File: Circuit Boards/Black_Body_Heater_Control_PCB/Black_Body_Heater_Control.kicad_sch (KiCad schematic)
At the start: 0 parts

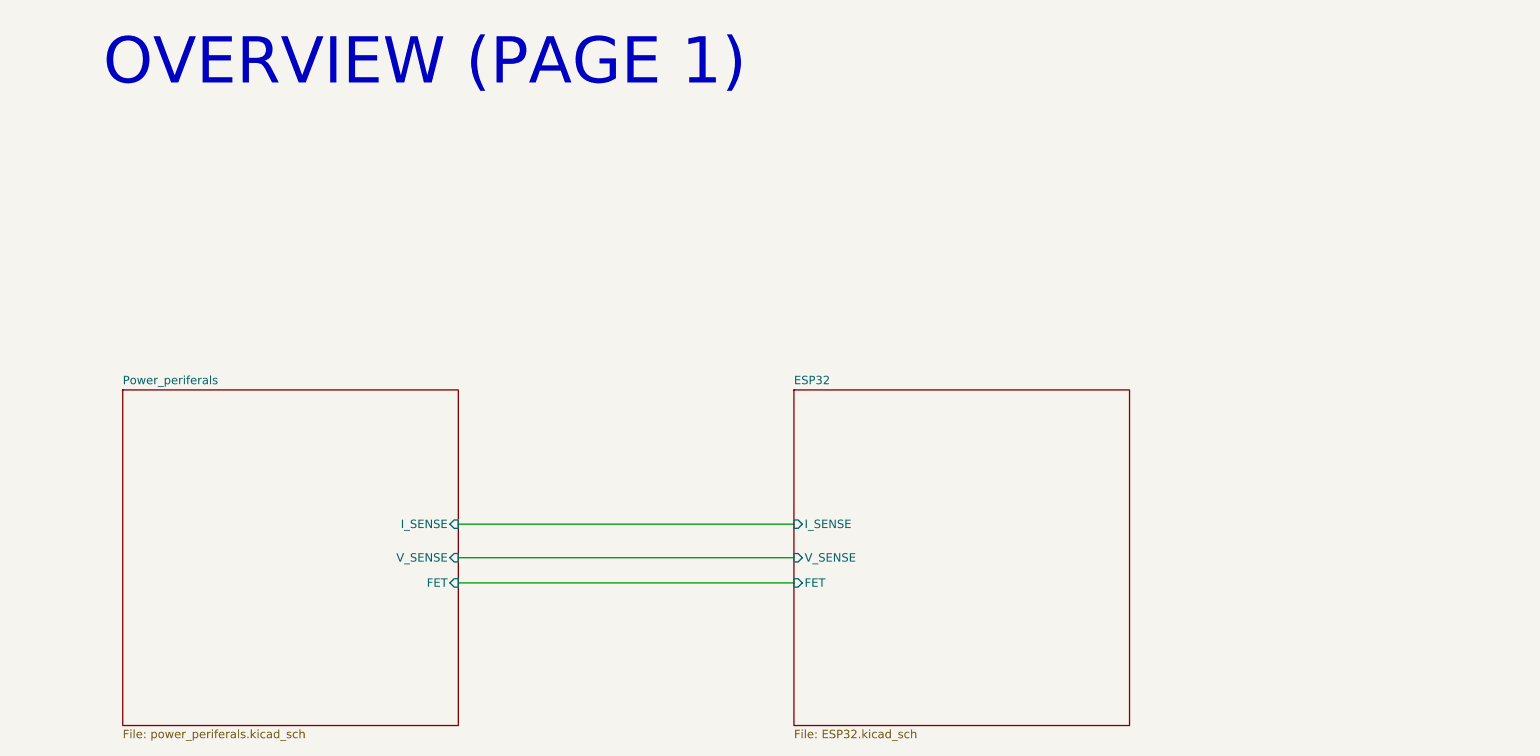
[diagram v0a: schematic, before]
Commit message: Heater PCB done (to review)
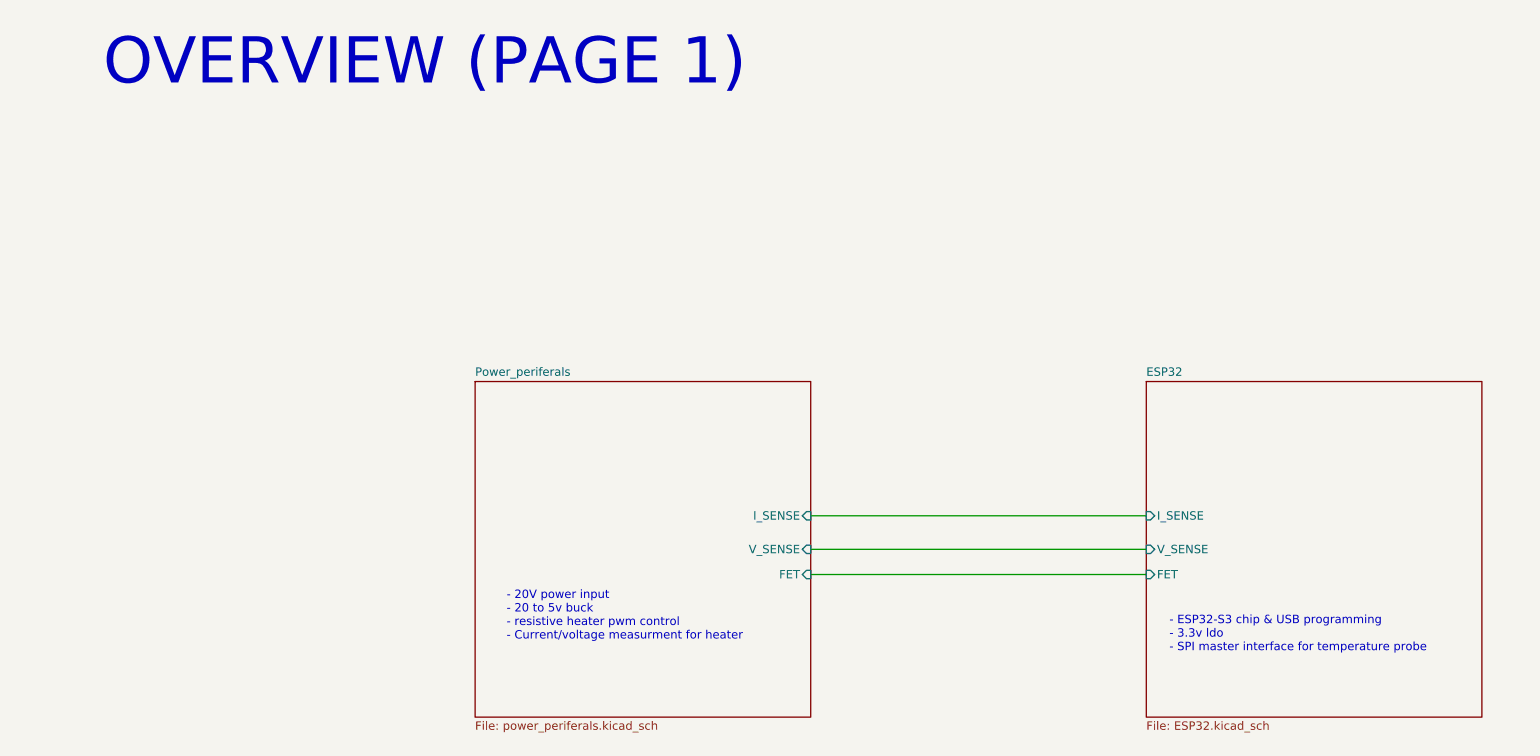
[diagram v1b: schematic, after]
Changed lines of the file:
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@@
+		)
+	)
+	(text_box "- ESP32-S3 chip & USB programming\n- 3.3v ldo\n- SPI master interface for temperature probe"
+		(exclude_from_sim no)
+		(at 182.88 109.22 0)
+		(size 48.26 13.97)
+		(margins 0.9525 0.9525 0.9525 0.9525)
+		(stroke
+			(width -0.0001)
+			(type solid)
+		)
+		(fill
+			(type none)
+		)
+		(effects
+			(font
+				(size 1.27 1.27)
+			)
+			(justify left top)
+		)
+	)
+	(text_box "- 20V power input\n- 20 to 5v buck\n- resistive heater pwm control\n- Current/voltage measurment for heater"
+		(exclude_from_sim no)
+		(at 82.55 105.41 0)
+		(size 43.18 13.97)
+		(margins 0.9525 0.9525 0.9525 0.9525)
+		(stroke
+			(width -0.0001)
+			(type solid)
+		)
+		(fill
+			(type none)
+		)
+		(effects
+			(font
+				(size 1.27 1.27)
+			)
+			(justify left top)
 		)
 	)
 	(wire
 		(pts
-			(xy 127 96.52) (xy 76.2 96.52)
+			(xy 180.34 95.25) (xy 129.54 95.25)
 		)
 		(stroke
@@
 	(wire
 		(pts
-			(xy 127 105.41) (xy 76.2 105.41)
+			(xy 180.34 104.14) (xy 129.54 104.14)
 		)
 		(stroke
@@
 	(wire
 		(pts
-			(xy 127 101.6) (xy 76.2 101.6)
+			(xy 180.34 100.33) (xy 129.54 100.33)
 		)
 		(stroke
@@
 	)
 	(sheet
-		(at 25.4 76.2)
+		(at 78.74 74.93)
 		(size 50.8 50.8)
 		(exclude_from_sim no)
@@
 		)
 		(property "Sheetname" "Power_periferals"
-			(at 25.4 75.4884 0)
+			(at 78.74 74.2184 0)
 			(show_name no)
 			(do_not_autoplace no)
@@
 		)
 		(property "Sheetfile" "power_periferals.kicad_sch"
-			(at 25.4 127.5846 0)
+			(at 78.74 126.3146 0)
 			(show_name no)
 			(do_not_autoplace no)
@@
 		)
 		(pin "FET" input
-			(at 76.2 105.41 0)
+			(at 129.54 104.14 0)
 			(effects
 				(font
@@
 		)
 		(pin "V_SENSE" input
-			(at 76.2 101.6 0)
+			(at 129.54 100.33 0)
 			(effects
 				(font
@@
 		)
 		(pin "I_SENSE" input
-			(at 76.2 96.52 0)
+			(at 129.54 95.25 0)
 			(effects
 				(font
@@
 	)
 	(sheet
-		(at 127 76.2)
+		(at 180.34 74.93)
 		(size 50.8 50.8)
 		(exclude_from_sim no)
@@
 		)
 		(property "Sheetname" "ESP32"
-			(at 127 75.4884 0)
+			(at 180.34 74.2184 0)
 			(show_name no)
 			(do_not_autoplace no)
@@
 		)
 		(property "Sheetfile" "ESP32.kicad_sch"
-			(at 127 127.5846 0)
+			(at 180.34 126.3146 0)
 			(show_name no)
 			(do_not_autoplace no)
@@
 		)
 		(pin "I_SENSE" input
-			(at 127 96.52 180)
+			(at 180.34 95.25 180)
 			(effects
 				(font
@@
 		)
 		(pin "FET" input
-			(at 127 105.41 180)
+			(at 180.34 104.14 180)
 			(effects
 				(font
@@
 		)
 		(pin "V_SENSE" input
-			(at 127 101.6 180)
+			(at 180.34 100.33 180)
 			(effects
 				(font

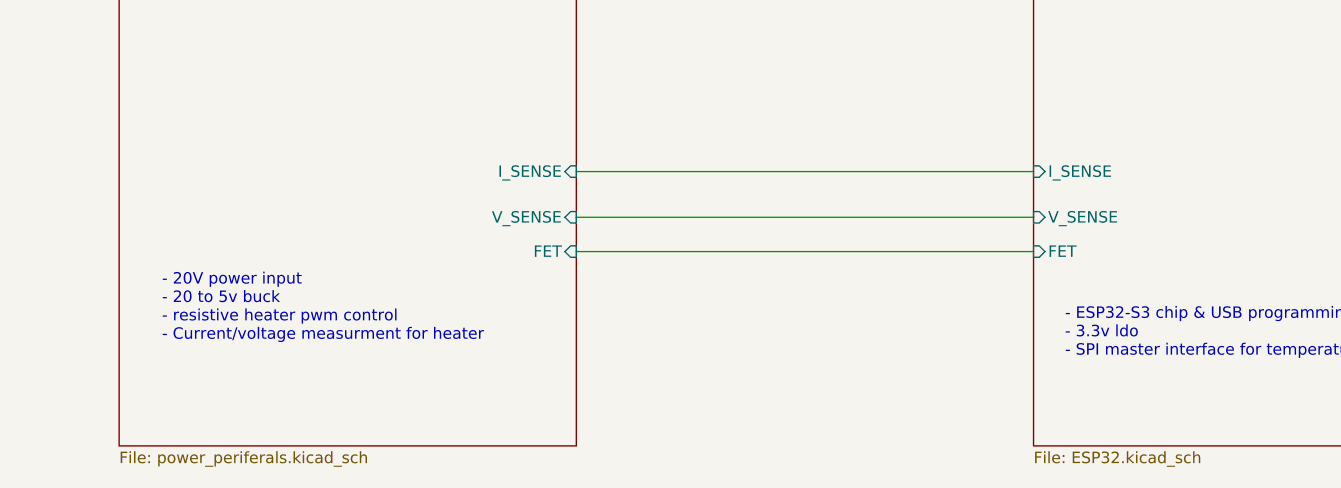
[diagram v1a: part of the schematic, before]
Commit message: Heater switched from pwm to vccs
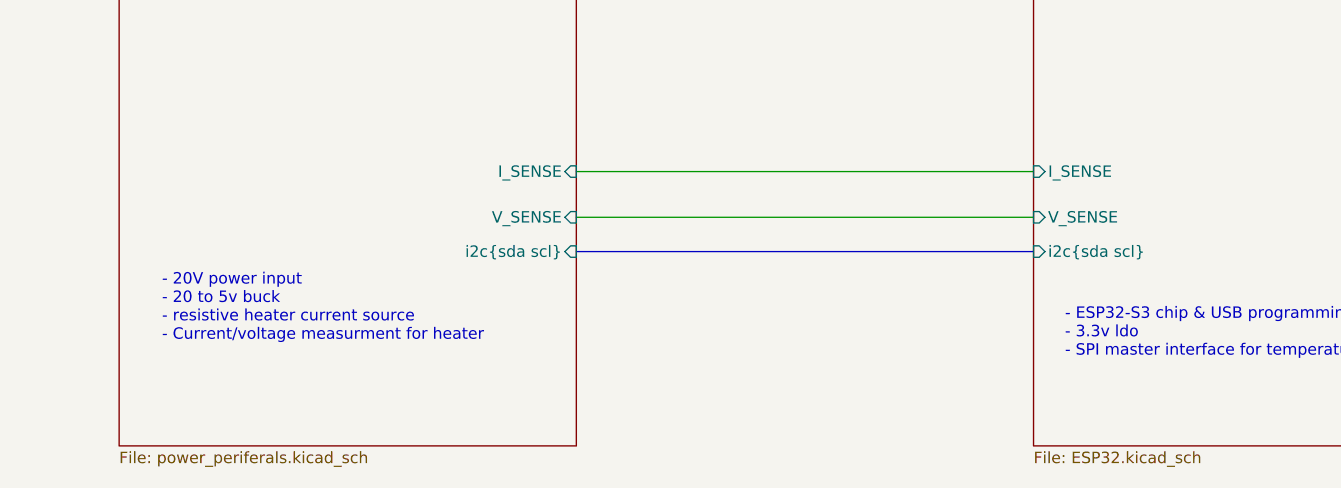
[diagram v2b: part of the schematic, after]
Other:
- sheet ESP32 ports: added i2c{sda scl}; removed FET
- sheet Power_periferals ports: added i2c{sda scl}; removed FET
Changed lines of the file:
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@@
 		)
 	)
-	(text_box "- 20V power input\n- 20 to 5v buck\n- resistive heater pwm control\n- Current/voltage measurment for heater"
+	(text_box "- 20V power input\n- 20 to 5v buck\n- resistive heater current source\n- Current/voltage measurment for heater"
 		(exclude_from_sim no)
 		(at 82.55 105.41 0)
@@
 		)
 	)
-	(wire
+	(bus
 		(pts
-			(xy 180.34 104.14) (xy 129.54 104.14)
+			(xy 129.54 104.14) (xy 180.34 104.14)
 		)
 		(stroke
@@
 			)
 		)
-		(pin "FET" input
-			(at 129.54 104.14 0)
-			(effects
-				(font
-					(size 1.27 1.27)
-				)
-				(justify right)
-			)
-		)
 		(pin "V_SENSE" input
 			(at 129.54 100.33 0)
@@
 		(pin "I_SENSE" input
 			(at 129.54 95.25 0)
+			(effects
+				(font
+					(size 1.27 1.27)
+				)
+				(justify right)
+			)
+		)
+		(pin "i2c{sda scl}" input
+			(at 129.54 104.14 0)
 			(effects
 				(font
@@
 			)
 		)
-		(pin "FET" input
-			(at 180.34 104.14 180)
+		(pin "V_SENSE" input
+			(at 180.34 100.33 180)
 			(effects
 				(font
@@
 			)
 		)
-		(pin "V_SENSE" input
-			(at 180.34 100.33 180)
+		(pin "i2c{sda scl}" input
+			(at 180.34 104.14 180)
 			(effects
 				(font
